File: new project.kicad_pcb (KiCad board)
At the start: 2 copper layers, 33.8 x 23 mm, 4 parts, among them J1 LED 0.170amps, J2 Tractive Battery

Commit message: Finally fixed
Please upload the changes
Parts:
- J2: footprint Resistor_SMD:R_0201_0603Metric -> Connector_Molex:Molex_Micro-Fit_3.0_43650-0200_1x02_P3.00mm_Horizontal
- R1: value 1800 -> 18000
- moved J2 15.7 mm to (135.5, 77.4), turned to 180 degrees
- moved U1 10.7 mm to (141.6, 63.3)
- moved R1 5.77 mm to (126.7, 63.5)
- moved J1 2.82 mm to (118.3, 66.9)
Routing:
- net Net-(J1-Pin_2): track 23.2 -> 122.2 mm
- net +4V: track 7.02 -> 68.7 mm
- net GND: track 11.8 -> 30.4 mm
- net Net-(U1-Cathode): track 3.48 -> 10.9 mm
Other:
- board size 33.8 x 23 mm -> 44.9 x 35 mm

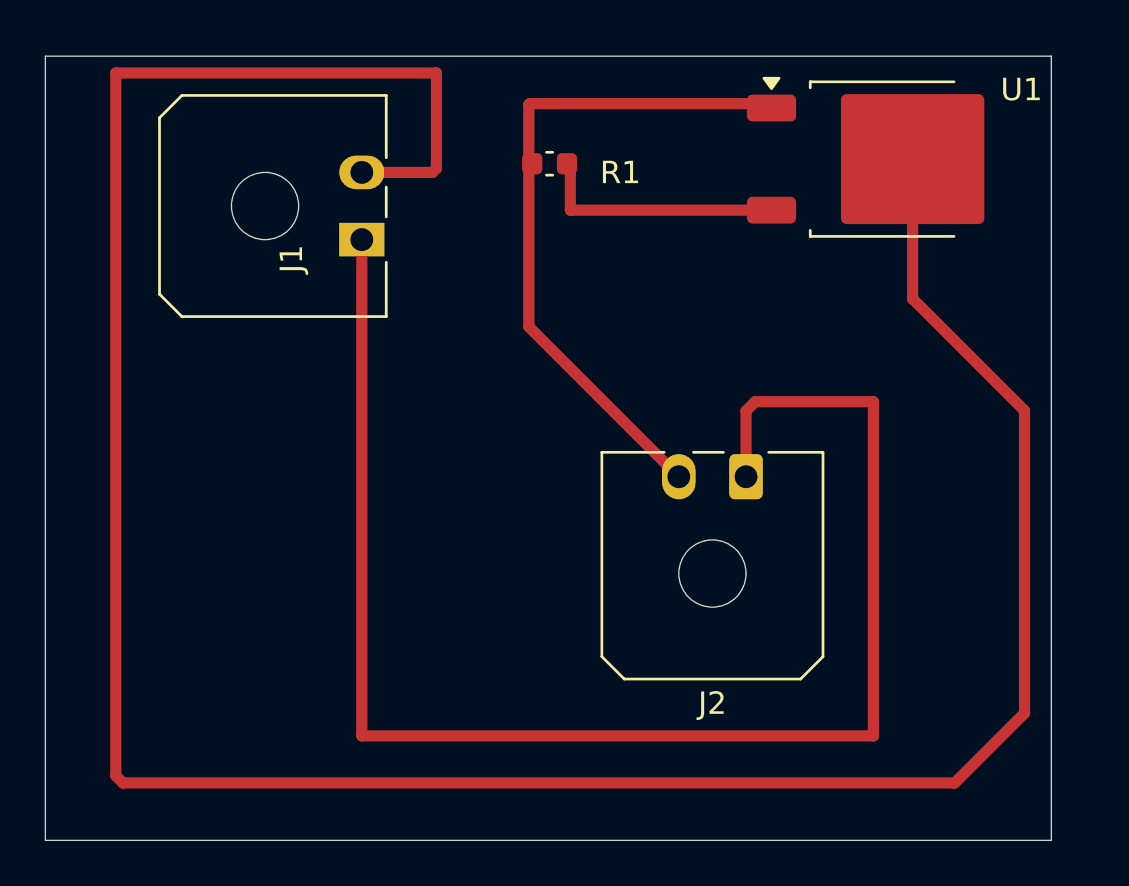
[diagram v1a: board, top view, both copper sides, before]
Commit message: Check
Redoing Wiring
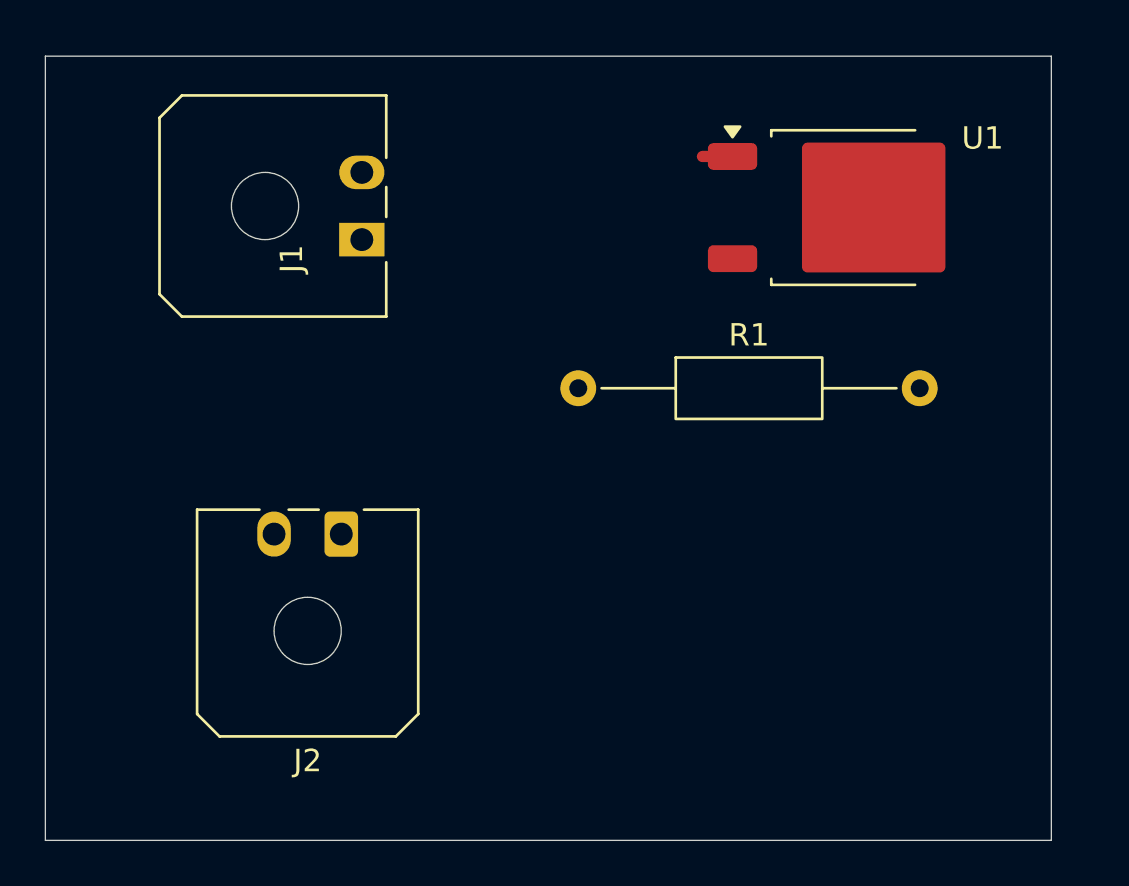
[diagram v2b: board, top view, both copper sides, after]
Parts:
- R1: footprint Capacitor_SMD:C_0603_1608Metric -> Resistor_THT:R_Axial_DIN0207_L6.3mm_D2.5mm_P15.24mm_Horizontal
- moved J2 18.2 mm to (117.4, 80.0)
- moved R1 10.1 mm to (128.0, 73.5)
- moved U1 2.77 mm to (139.9, 65.4)
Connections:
- net +4V renamed +BATT
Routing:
- net Net-(J1-Pin_2): track 122.2 -> 0.00 mm
- net +BATT: track 68.7 -> 0.00 mm
- net GND: track 30.4 -> 1.71 mm
- net Net-(U1-Cathode): track 10.9 -> 0.00 mm

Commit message: FInished
Done
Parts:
- removed J1: LED 0.170amps, Connector_Molex:Molex_Micro-Fit_3.0_43650-0200_1x02_P3.00mm_Horizontal
- removed J2: Tractive Battery, Connector_Molex:Molex_Micro-Fit_3.0_43650-0200_1x02_P3.00mm_Horizontal
- removed R1: 18000, Resistor_THT:R_Axial_DIN0207_L6.3mm_D2.5mm_P15.24mm_Horizontal
- removed U1: ~, Package_TO_SOT_SMD:TO-252-2
- added H1: MountingHole, MountingHole:MountingHole_2.1mm, F.Cu at (110.6, 75.7)
- added H2: MountingHole, MountingHole:MountingHole_2.1mm, F.Cu at (144.1, 75.8)
- added J3: Tractive Battery, Connector_Molex:Molex_Micro-Fit_3.0_43650-0200_1x02_P3.00mm_Horizontal, F.Cu at (116.9, 68.7)
- added J4: LED 0.170amps, Connector_Molex:Molex_Micro-Fit_3.0_43650-0200_1x02_P3.00mm_Horizontal, F.Cu at (137.9, 66.5)
- added R2: 18000, Resistor_THT:R_Axial_DIN0207_L6.3mm_D2.5mm_P10.16mm_Horizontal, F.Cu at (123.1, 71.6)
- added U2: ~, Package_TO_SOT_SMD:TO-252-2, F.Cu at (127.7, 65.0)
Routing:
- net Net-(J3-Pin_2): track 0.00 -> 21.3 mm
- net GND: track 1.71 -> 16.3 mm
- net Net-(U2-Cathode): track 0.00 -> 12.4 mm
- net Net-(J4-Pin_2): track 0.00 -> 10.8 mm
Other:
- board size 44.9 x 35 mm -> 44.9 x 23.4 mm
